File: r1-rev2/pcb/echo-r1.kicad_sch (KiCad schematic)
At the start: 95 parts, among them J2 TYPE-C-31-M-12, J3 TF-115, J6 Conn_01x05, J7 ILI9342C, J8 Conn_01x04, Q4 AO3401A, Q5 AO3401A, SW1 POWER, SW10 DPAD→, SW11 START, SW12 SELECT, SW13 VOL+, SW14 VOL-, SW2 HOLD, SW3 A, SW4 B, SW5 X, SW6 Y, SW7 DPAD↑, SW8 DPAD↓, SW9 DPAD←, U10 TPAZ1143-04F, U11 TPAZ1143-04F, U12 TPAZ1143-04F, U14 USBLC6-2SC6, U16 SY7200A, U7 STM32H7R3Z8Jx, U8 W958D8NBYA5I, U9 TPAZ1143-04F, Y1 SC-32S32.768kHz20PPM12.5pF, Y2 XTM32024000JT00351001

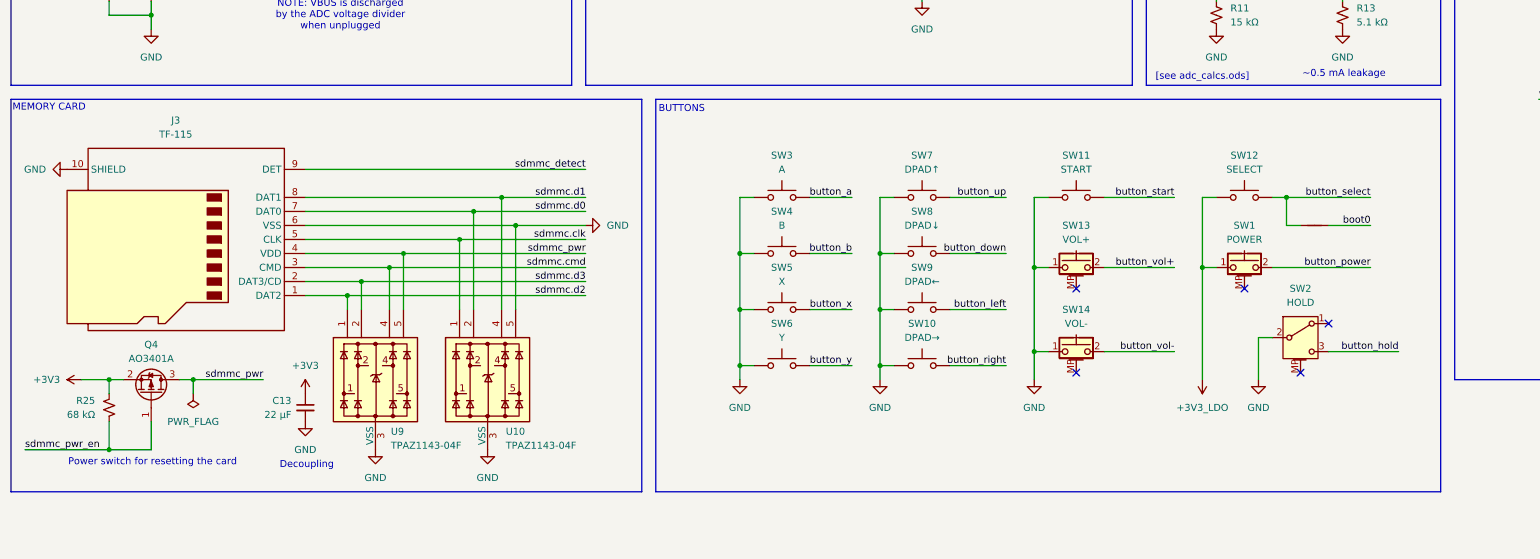
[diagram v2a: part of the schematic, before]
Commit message: R1-Rev2: initial mechanical layout
- Outline front side of case, LCD module, and cable
- Lay out LCD, since it requires 12'oclock viewing angle a slot is
  required to thread the ribbon cable through to the back plane.
- Place buttons, HP/LO jacks, and USB port
- Make the power/volume buttons larger
- Remove old button footprints
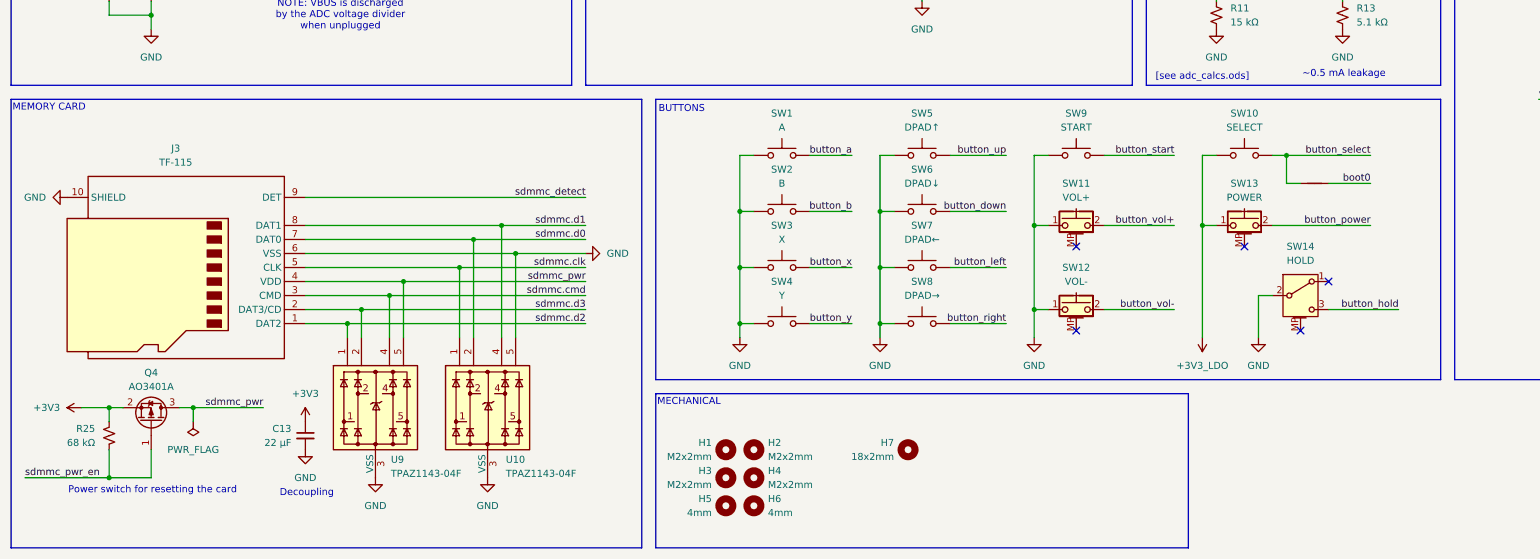
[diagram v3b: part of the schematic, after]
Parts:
- added H1, H2, H3, H4: M2x2mm, MountingHole:MountingHole_2.2mm_M2, symbol Mechanical:MountingHole
- added H5, H6: 4mm, MountingHole:MountingHole_4mm, symbol Mechanical:MountingHole
- added H7: 18x2mm, echoplayer:Slot_18x2mm, symbol Mechanical:MountingHole
- SW11: renamed from SW13; footprint echoplayer:Switch_XKB_TS-1010-C-A -> echoplayer:Switch_HROPARTS_K2-1112SA-A4DW-01
- SW12: renamed from SW14; footprint echoplayer:Switch_XKB_TS-1010-C-A -> echoplayer:Switch_HROPARTS_K2-1112SA-A4DW-01
- SW13: renamed from SW1; footprint echoplayer:Switch_XKB_TS-1010-C-A -> echoplayer:Switch_HROPARTS_K2-1112SA-A4DW-01
- renumbered SW3 to SW1, SW12 to SW10, SW2 to SW14, SW4 to SW2, SW5 to SW3, SW6 to SW4, SW7 to SW5, SW8 to SW6, SW9 to SW7, SW10 to SW8, SW11 to SW9
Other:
- note added: "MECHANICAL"
- moved on the sheet: C13, J3, Q4, R25, SW1, SW10, SW11, SW12, SW13, SW14, SW2, SW3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

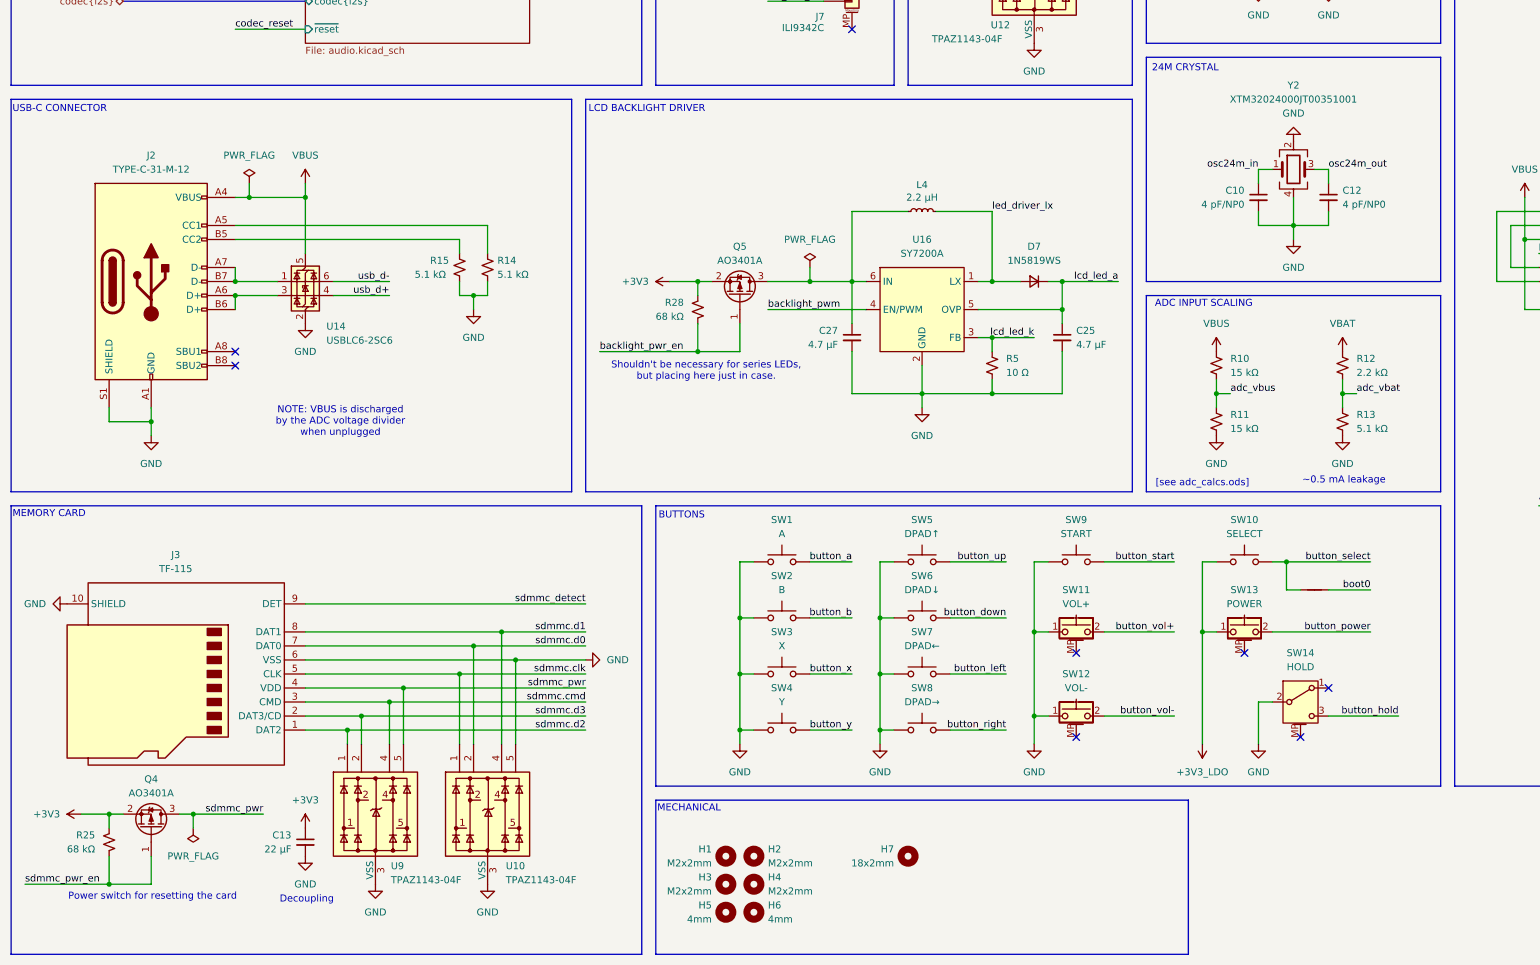
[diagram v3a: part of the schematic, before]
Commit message: R1-Rev2: update backlight driver circuit
There are 4 LEDs in parallel in the LCD backlight, sharing the
same cathode/anode, so the backlight can be driven with just a
MOSFET and resistor. (A PMOS is used to avoid having to add a
new unique component.)
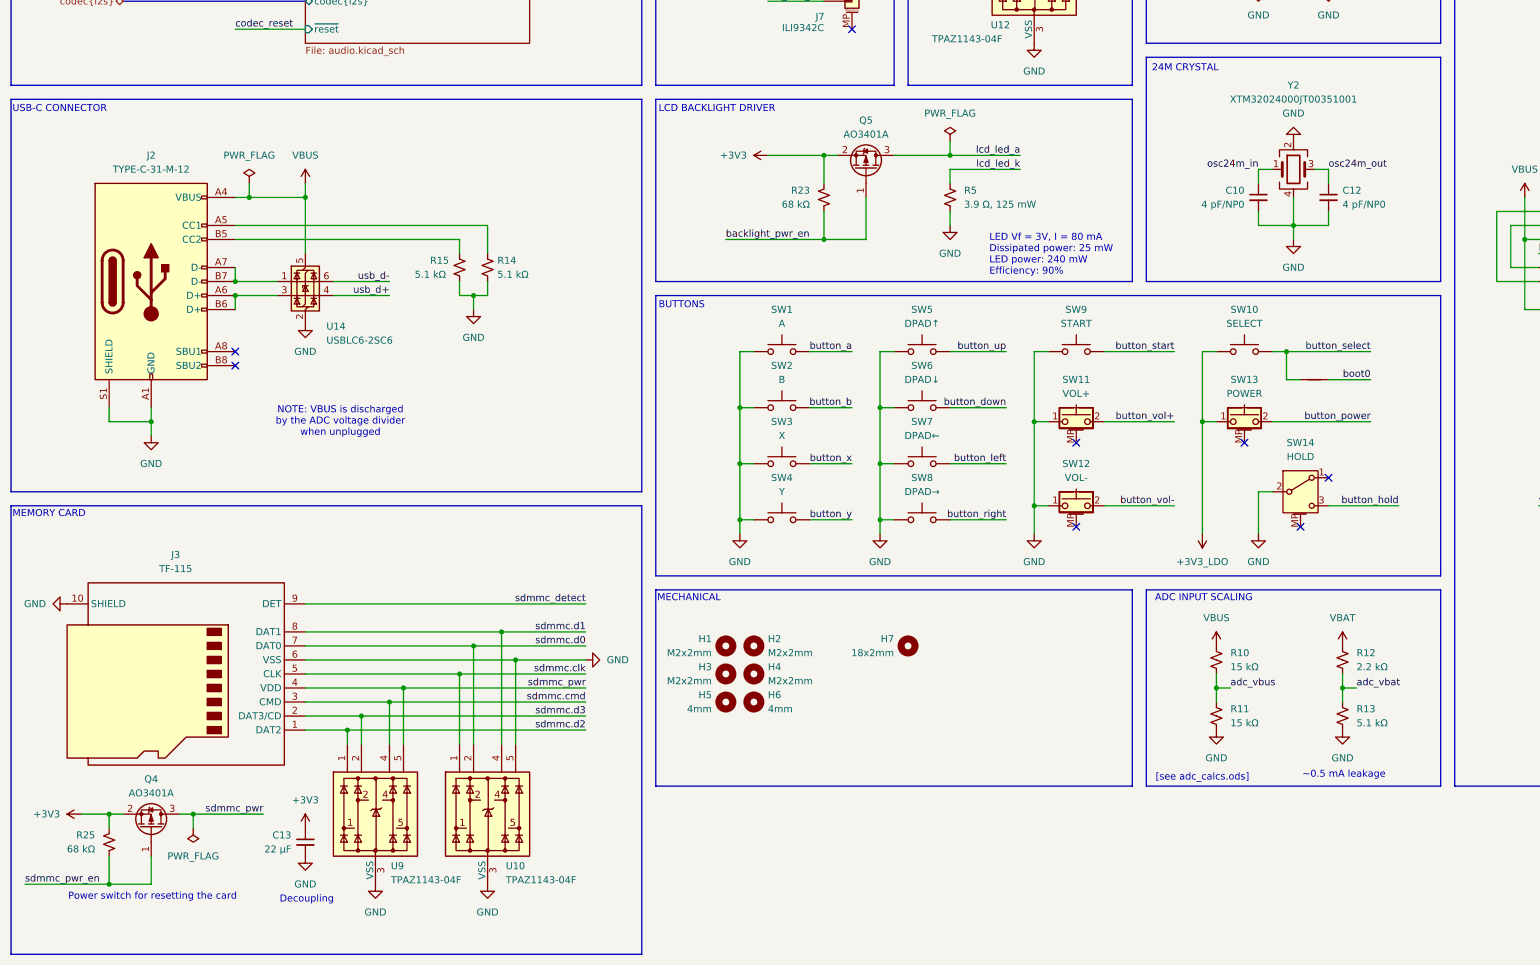
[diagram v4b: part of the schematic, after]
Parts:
- removed C25, C27: 4.7 µF, Capacitor_SMD:C_0402_1005Metric, symbol Device:C_Small
- removed D7: 1N5819WS, Diode_SMD:D_SOD-323, symbol Device:D_Small
- removed L4: 2.2 µH, symbol Device:L_Small
- removed R28: 68 kΩ, Resistor_SMD:R_0402_1005Metric, symbol Device:R_Small_US
- removed U16: SY7200A, Package_TO_SOT_SMD:SOT-23-6, symbol echoplayer:SY7200A
- added R23: 68 kΩ, Resistor_SMD:R_0402_1005Metric, symbol Device:R_Small_US
- R5: value 10 Ω -> 3.9 Ω, 125 mW
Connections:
- net +3V3: now also R23.1
- net backlight_pwr_en: now also R23.2
- net lcd_led_a: now also Q5.3 (D)
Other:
- note added: "LED Vf = 3V, I = 80 mA Dissipated power: 25 mW LED power: 240 mW Efficiency: 90%"
- note removed: "Shouldn't be necessary for series LEDs, but placing here just in case."
- moved on the sheet: H1, H2, H3, H4, H5, H6, H7, Q5, R10, R11, R12, R13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

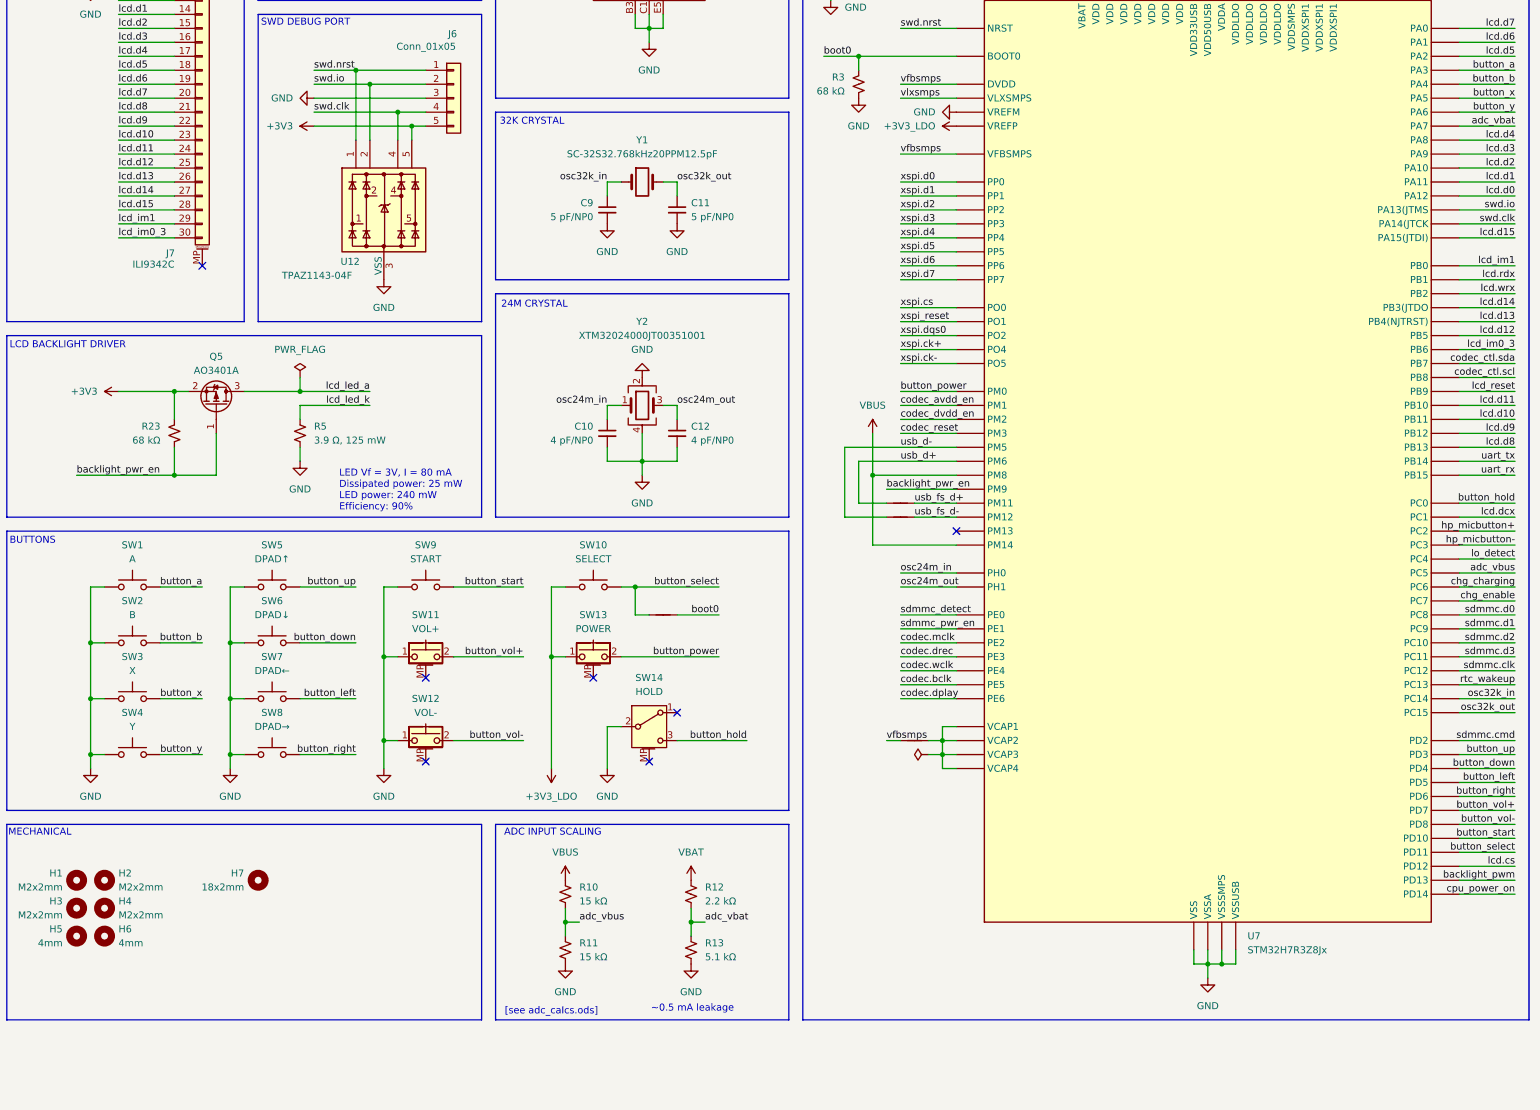
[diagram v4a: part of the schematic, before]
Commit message: R1-Rev2: use FMC NAND mode for 8-bit 8080 LCD interface
NAND mode will translate 16-bit AXI transfers into two
8-bit FMC transfers, which allows the 8-bit LCD bus to
work with DMA2D. The NWAIT pin does need to be "wasted"
on a fixed 3v3 input, since the FMC expects to poll it
(normally it would be the busy signal from a NAND chip).

It's seems likely this can be disabled by clearing the
PWAITEN bit so I've added a solder jumper to test it.

This saves 7 pins off the LCD data bus. The IM pins are
now fixed which saves another 2 pins.
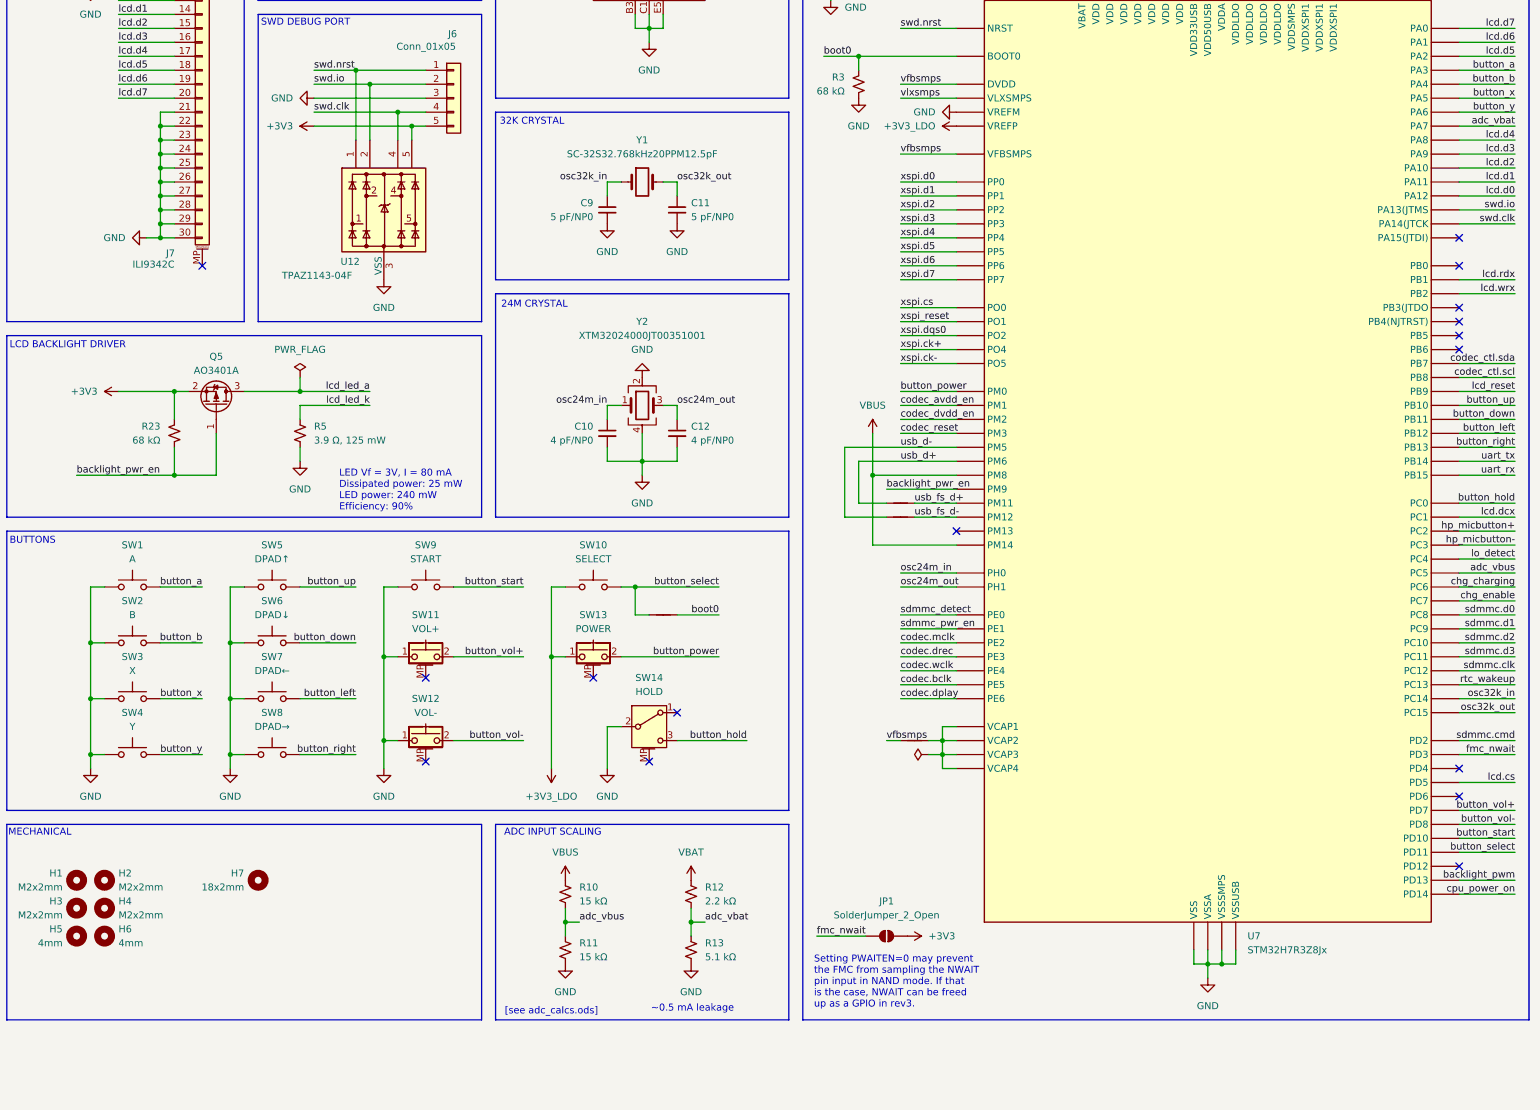
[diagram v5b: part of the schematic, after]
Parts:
- added JP1: SolderJumper_2_Open, Jumper:SolderJumper-2_P1.3mm_Open_RoundedPad1.0x1.5mm, symbol Jumper:SolderJumper_2_Open
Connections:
- net +3V3: now also JP1.2 (B)
- net GND: now also J7.21 (Pin_21), J7.22 (Pin_22), J7.23 (Pin_23), J7.24 (Pin_24), J7.25 (Pin_25), J7.26 (Pin_26), J7.27 (Pin_27), J7.28 (Pin_28), J7.29 (Pin_29), J7.30 (Pin_30)
- net button_down: now also U7.K12 (PB11); no longer U7.B12 (PD4)
- net button_left: now also U7.H10 (PB12); no longer U7.B6 (PD5)
- net button_right: now also U7.J11 (PB13); no longer U7.C6 (PD6)
- net button_up: now also U7.J10 (PB10); no longer U7.D10 (PD3)
- net lcd.cs: now also U7.B6 (PD5); no longer U7.K11 (PD12)
- removed net lcd.d10: J7.23 (Pin_23), U7.K12 (PB11)
- removed net lcd.d11: J7.24 (Pin_24), U7.J10 (PB10)
- net lcd.d12: no longer names the net of U7.A4 (PB5)
- net lcd.d12: no longer J7.25 (Pin_25)
- net lcd.d13: no longer names the net of U7.C5 (PB4(NJTRST))
- net lcd.d13: no longer J7.26 (Pin_26)
- net lcd.d14: no longer names the net of U7.B5 (PB3(JTDO)
- net lcd.d14: no longer J7.27 (Pin_27)
- net lcd.d15: no longer names the net of U7.D12 (PA15(JTDI))
- net lcd.d15: no longer J7.28 (Pin_28)
- removed net lcd.d8: J7.21 (Pin_21), U7.J11 (PB13)
- removed net lcd.d9: J7.22 (Pin_22), U7.H10 (PB12)
- net lcd_im0_3: no longer names the net of U7.A3 (PB6)
- net lcd_im0_3: no longer J7.30 (Pin_30)
- net lcd_im1: no longer names the net of U7.L4 (PB0)
- net lcd_im1: no longer J7.29 (Pin_29)
- new net fmc_nwait: JP1.1 (A), U7.D10 (PD3)
- no-connect marks 10 -> 19
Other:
- note added: "Setting PWAITEN=0 may prevent the FMC from sampling the NWAIT pin input in NAND mode. If that is the case, NWAIT can be freed up as a GPIO in rev3."
